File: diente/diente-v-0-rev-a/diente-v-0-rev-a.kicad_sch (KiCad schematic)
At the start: 3 parts, among them J1 Conn_02x05_Odd_Even

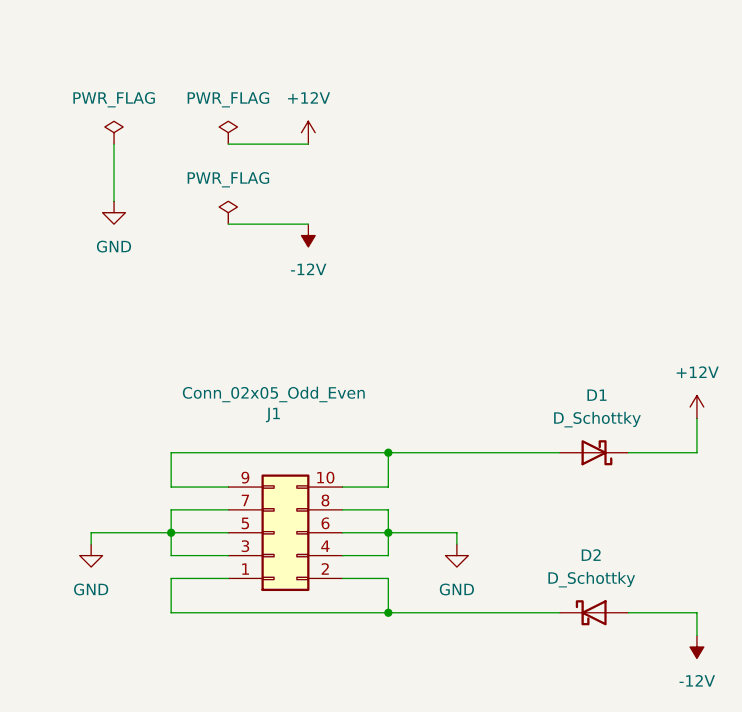
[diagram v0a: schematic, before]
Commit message: agregar alimentacion a diente
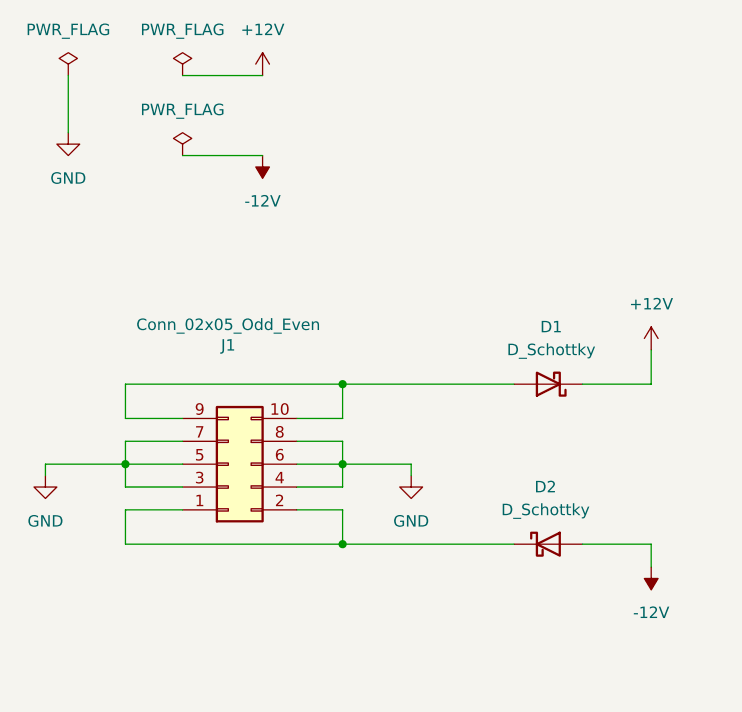
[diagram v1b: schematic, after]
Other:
- title: fuente-alimentacion -> (none)
- moved on the sheet: D1, D2, J1
